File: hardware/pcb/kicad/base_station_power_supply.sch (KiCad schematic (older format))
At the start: 18 parts, among them CON1 CONN_2, IC1 BRIDGE_TART

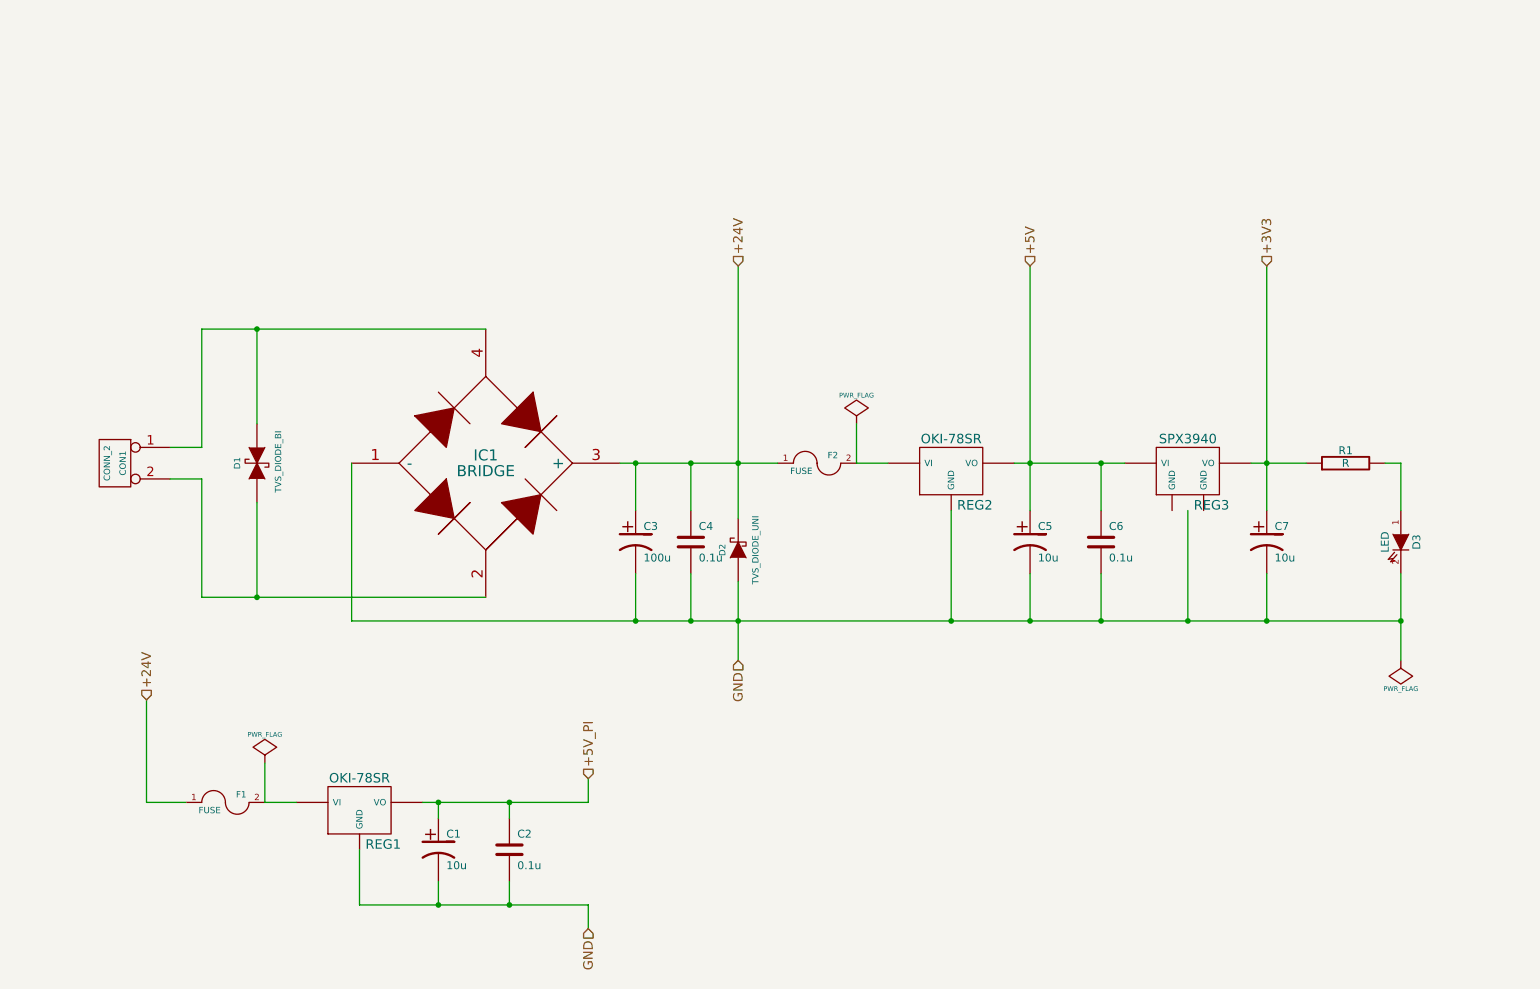
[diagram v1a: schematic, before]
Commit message: Added a power switch
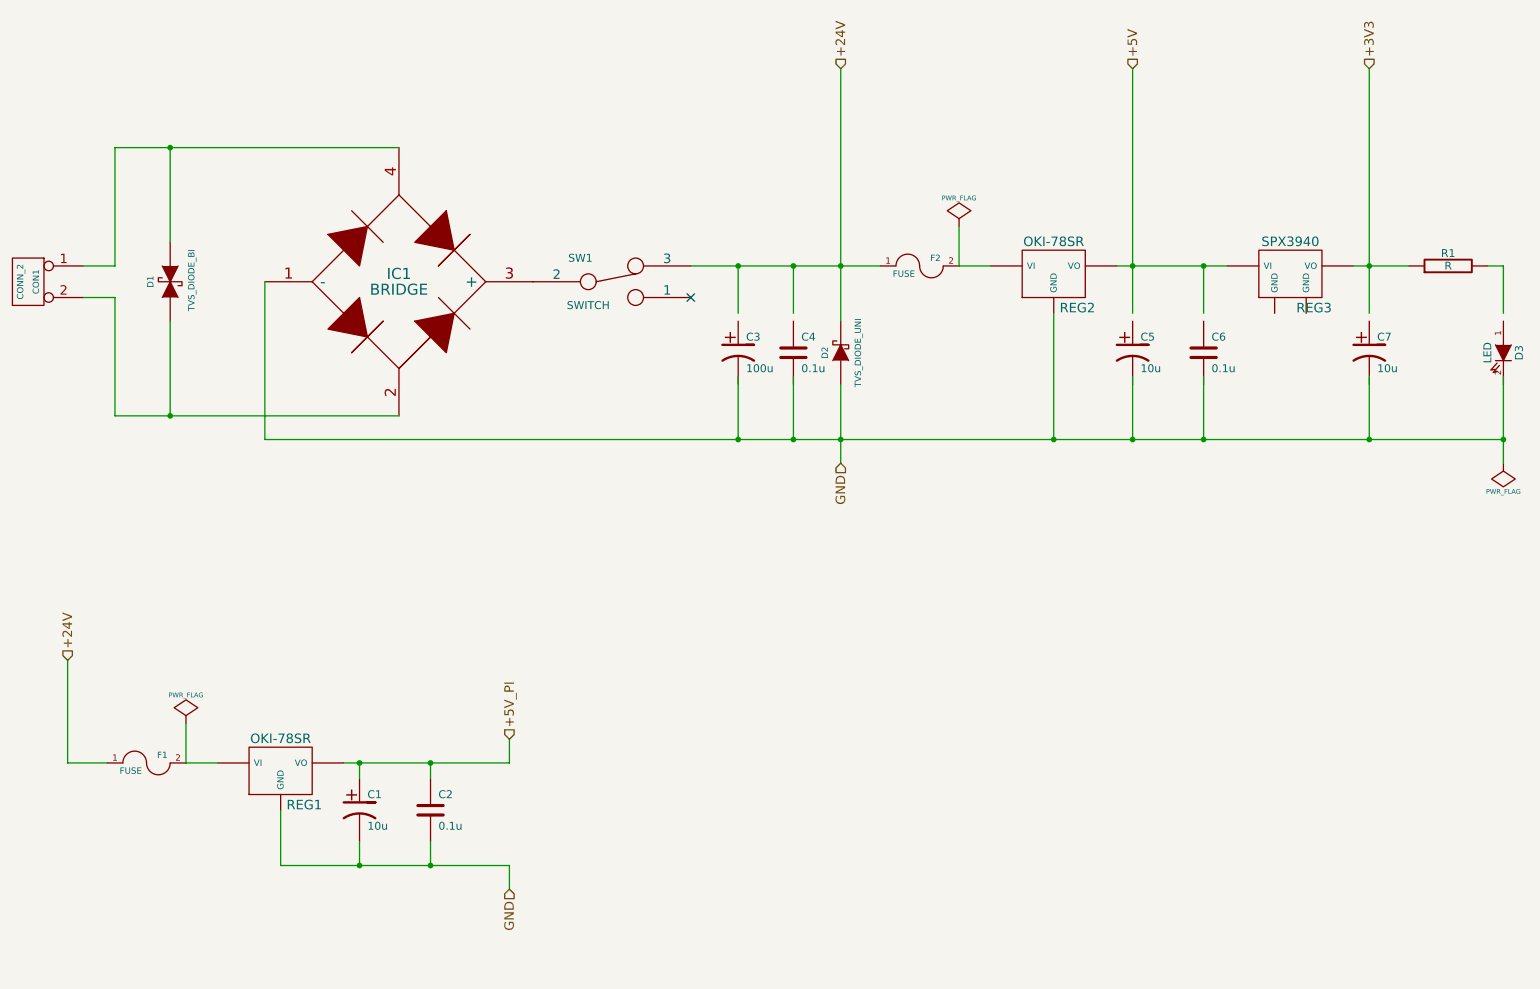
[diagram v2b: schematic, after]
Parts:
- added SW1: SWITCH, CS12ANW03_TART, symbol SWITCH
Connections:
- wire segments 45 -> 44
- no-connect marks 0 -> 1
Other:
- moved on the sheet: C1, C2, C3, C4, C5, C6, C7, CON1, D1, D2, D3, F1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

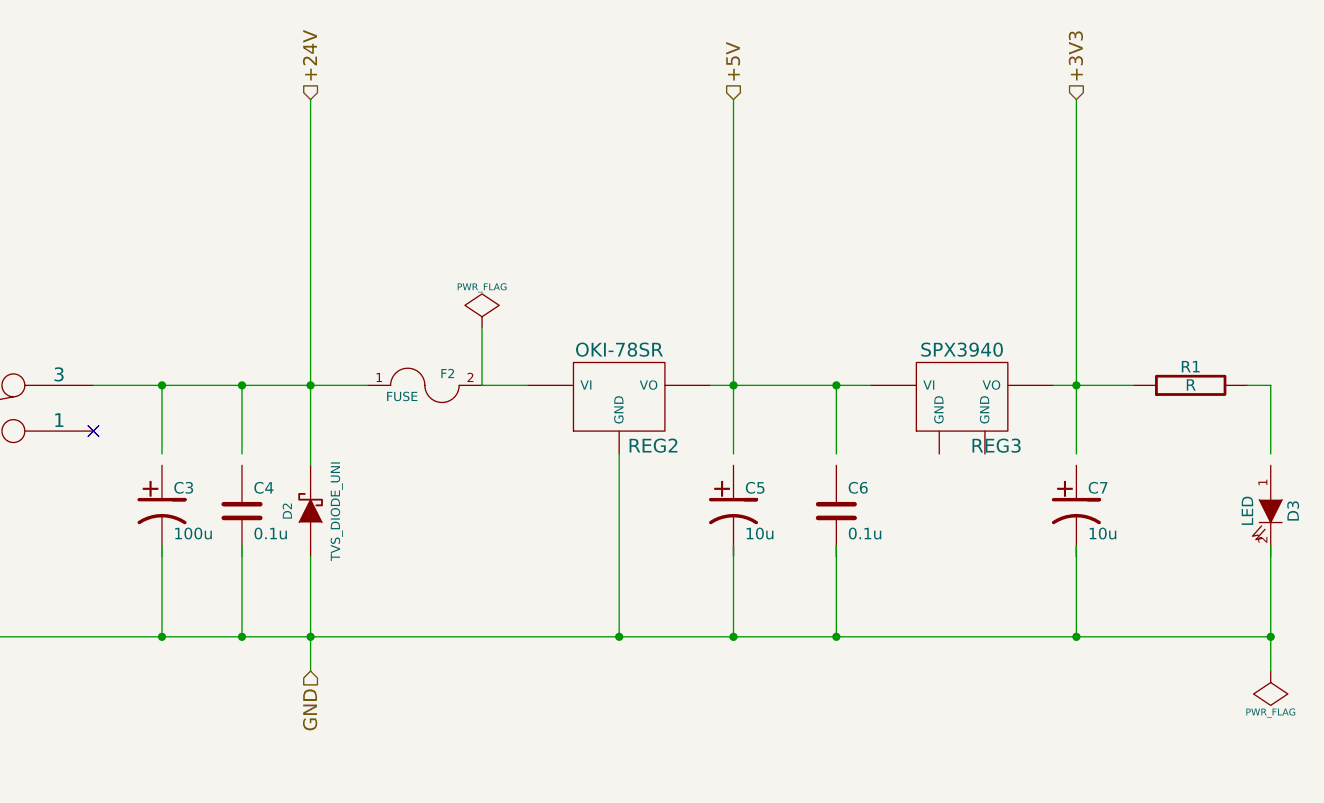
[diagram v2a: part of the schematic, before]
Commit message: Base station and radio hub boards ready for final checks before manufacture
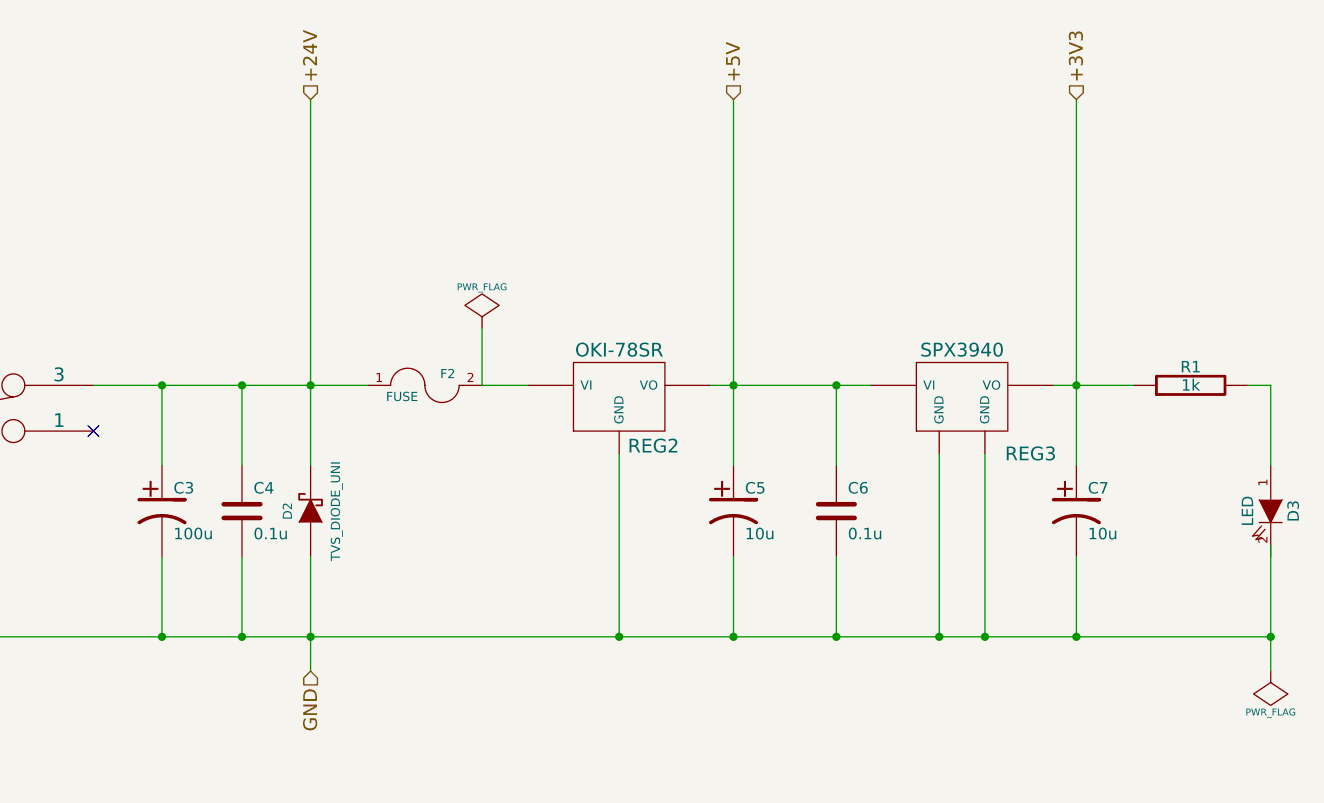
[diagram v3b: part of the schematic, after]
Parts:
- R1: value R -> 1k
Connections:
- wire segments 44 -> 46
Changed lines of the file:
@@
 Sheet 2 7
 Title ""
-Date "13 nov 2014"
+Date "4 dec 2014"
 Rev ""
 Comp ""
@@
 U 1 1 5419032C
 P 9100 2400
-F 0 "REG3" H 9250 2184 60  0000 C CNN
+F 0 "REG3" H 9400 2150 60  0000 C CNN
 F 1 "SPX3940_TART" H 9100 2710 60  0001 C CNN
 F 2 "" H 9100 2400 60  0001 C CNN
@@
 P 10100 2350
 F 0 "R1" V 10180 2350 50  0000 C CNN
-F 1 "R" V 10100 2350 50  0000 C CNN
+F 1 "1k" V 10100 2350 50  0000 C CNN
 F 2 "" H 10100 2350 60  0001 C CNN
 F 3 "" H 10100 2350 60  0001 C CNN
@@
 $EndComp
 NoConn ~ 5300 2550
-Connection ~ 5600 3450
-Wire Wire Line
-	5600 3050 5600 3450
-Connection ~ 5950 3450
-Wire Wire Line
-	5950 3450 5950 3050
-Wire Wire Line
-	6250 3100 6250 3600
-Connection ~ 7600 3450
-Wire Wire Line
-	7600 3450 7600 2650
-Connection ~ 8100 3450
-Wire Wire Line
-	8100 3450 8100 3050
-Connection ~ 8550 3450
-Wire Wire Line
-	8550 3450 8550 3050
-Connection ~ 9600 3450
-Wire Wire Line
-	9600 3450 9600 3050
-Connection ~ 10450 3450
-Wire Wire Line
-	2600 3450 10450 3450
-Wire Wire Line
-	2700 6150 4150 6150
-Wire Wire Line
-	3100 5500 4150 5500
-Wire Wire Line
-	4150 5500 4150 5350
-Wire Wire Line
-	1350 5500 1350 4850
-Wire Wire Line
-	10450 3050 10450 3600
-Wire Wire Line
-	9600 1100 9600 2650
-Connection ~ 6250 2350
-Connection ~ 5950 2350
-Wire Wire Line
-	5950 2350 5950 2650
-Connection ~ 2000 3300
-Wire Wire Line
-	1650 3300 3450 3300
-Wire Wire Line
-	1650 2550 1650 3300
-Wire Wire Line
-	2000 2700 2000 3300
-Wire Wire Line
-	1450 2550 1650 2550
-Connection ~ 9600 2350
-Wire Wire Line
-	9500 2350 9850 2350
-Connection ~ 8550 2350
-Wire Wire Line
-	8550 2350 8550 2650
-Wire Wire Line
-	8000 2350 8700 2350
-Connection ~ 8100 2350
-Wire Wire Line
-	10450 2350 10350 2350
-Wire Wire Line
-	10450 2650 10450 2350
-Wire Wire Line
-	7000 2350 7200 2350
-Wire Wire Line
-	1650 2350 1450 2350
-Wire Wire Line
-	2000 2200 2000 1600
-Wire Wire Line
-	1650 1600 1650 2350
-Wire Wire Line
-	1650 1600 3450 1600
-Connection ~ 2000 1600
-Wire Wire Line
-	2600 3450 2600 2450
-Wire Wire Line
-	5600 2350 5600 2650
-Connection ~ 5600 2350
-Wire Wire Line
-	5300 2350 6500 2350
-Wire Wire Line
-	7000 2100 7000 2350
-Wire Wire Line
-	8100 1100 8100 2650
-Wire Wire Line
-	2100 5500 2100 5250
-Wire Wire Line
-	2300 5500 2100 5500
-Connection ~ 3650 6150
-Wire Wire Line
-	3650 6150 3650 6000
-Connection ~ 3200 5500
-Wire Wire Line
-	3650 5500 3650 5600
-Connection ~ 3650 5500
-Wire Wire Line
-	3200 6000 3200 6150
-Wire Wire Line
-	3200 5600 3200 5500
-Wire Wire Line
-	1600 5500 1350 5500
-Wire Wire Line
-	2700 5800 2700 6150
-Connection ~ 3200 6150
-Wire Wire Line
-	4150 6150 4150 6300
-Wire Wire Line
-	6250 1100 6250 2700
 $Comp
 L SWITCH SW1
@@
 	1    0    0    -1
 $EndComp
+Connection ~ 5600 3450
+Wire Wire Line
+	5600 3100 5600 3450
+Connection ~ 5950 3450
+Wire Wire Line
+	5950 3450 5950 3100
+Wire Wire Line
+	6250 3100 6250 3600
+Connection ~ 7600 3450
+Wire Wire Line
+	7600 3450 7600 2650
+Connection ~ 8100 3450
+Wire Wire Line
+	8100 3450 8100 3100
+Connection ~ 8550 3450
+Wire Wire Line
+	8550 3450 8550 3100
+Connection ~ 9600 3450
+Connection ~ 10450 3450
+Wire Wire Line
+	2600 3450 10450 3450
+Wire Wire Line
+	2700 6150 4150 6150
+Wire Wire Line
+	3100 5500 4150 5500
+Wire Wire Line
+	4150 5500 4150 5350
+Wire Wire Line
+	1350 5500 1350 4850
+Wire Wire Line
+	10450 3050 10450 3600
+Wire Wire Line
+	9600 1100 9600 2700
+Connection ~ 6250 2350
+Connection ~ 5950 2350
+Wire Wire Line
+	5950 2350 5950 2700
+Connection ~ 2000 3300
+Wire Wire Line
+	1650 3300 3450 3300
+Wire Wire Line
+	1650 2550 1650 3300
+Wire Wire Line
+	2000 2700 2000 3300
+Wire Wire Line
+	1450 2550 1650 2550
+Connection ~ 9600 2350
+Wire Wire Line
+	9500 2350 9850 2350
+Connection ~ 8550 2350
+Wire Wire Line
+	8550 2350 8550 2700
+Wire Wire Line
+	8000 2350 8700 2350
+Connection ~ 8100 2350
+Wire Wire Line
+	10450 2350 10350 2350
+Wire Wire Line
+	10450 2700 10450 2350
+Wire Wire Line
+	7000 2350 7200 2350
+Wire Wire Line
+	1650 2350 1450 2350
+Wire Wire Line
+	2000 2200 2000 1600
+Wire Wire Line
+	1650 1600 1650 2350
+Wire Wire Line
+	1650 1600 3450 1600
+Connection ~ 2000 1600
+Wire Wire Line
+	2600 3450 2600 2450
+Wire Wire Line
+	5600 2350 5600 2700
+Connection ~ 5600 2350
+Wire Wire Line
+	5300 2350 6500 2350
+Wire Wire Line
+	7000 2100 7000 2350
+Wire Wire Line
+	8100 1100 8100 2700
+Wire Wire Line
+	2100 5500 2100 5250
+Wire Wire Line
+	2300 5500 2100 5500
+Connection ~ 3650 6150
+Wire Wire Line
+	3650 6150 3650 6000
+Connection ~ 3200 5500
+Wire Wire Line
+	3650 5500 3650 5600
+Connection ~ 3650 5500
+Wire Wire Line
+	3200 6000 3200 6150
+Wire Wire Line
+	3200 5600 3200 5500
+Wire Wire Line
+	1600 5500 1350 5500
+Wire Wire Line
+	2700 5800 2700 6150
+Connection ~ 3200 6150
+Wire Wire Line
+	4150 6150 4150 6300
+Wire Wire Line
+	6250 1100 6250 2700
 Connection ~ 6250 3450
+Wire Wire Line
+	9600 3100 9600 3450
+Wire Wire Line
+	9000 2650 9000 3450
+Connection ~ 9000 3450
+Wire Wire Line
+	9200 2650 9200 3450
+Connection ~ 9200 3450
 $EndSCHEMATC
